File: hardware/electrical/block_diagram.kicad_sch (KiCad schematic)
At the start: 0 parts

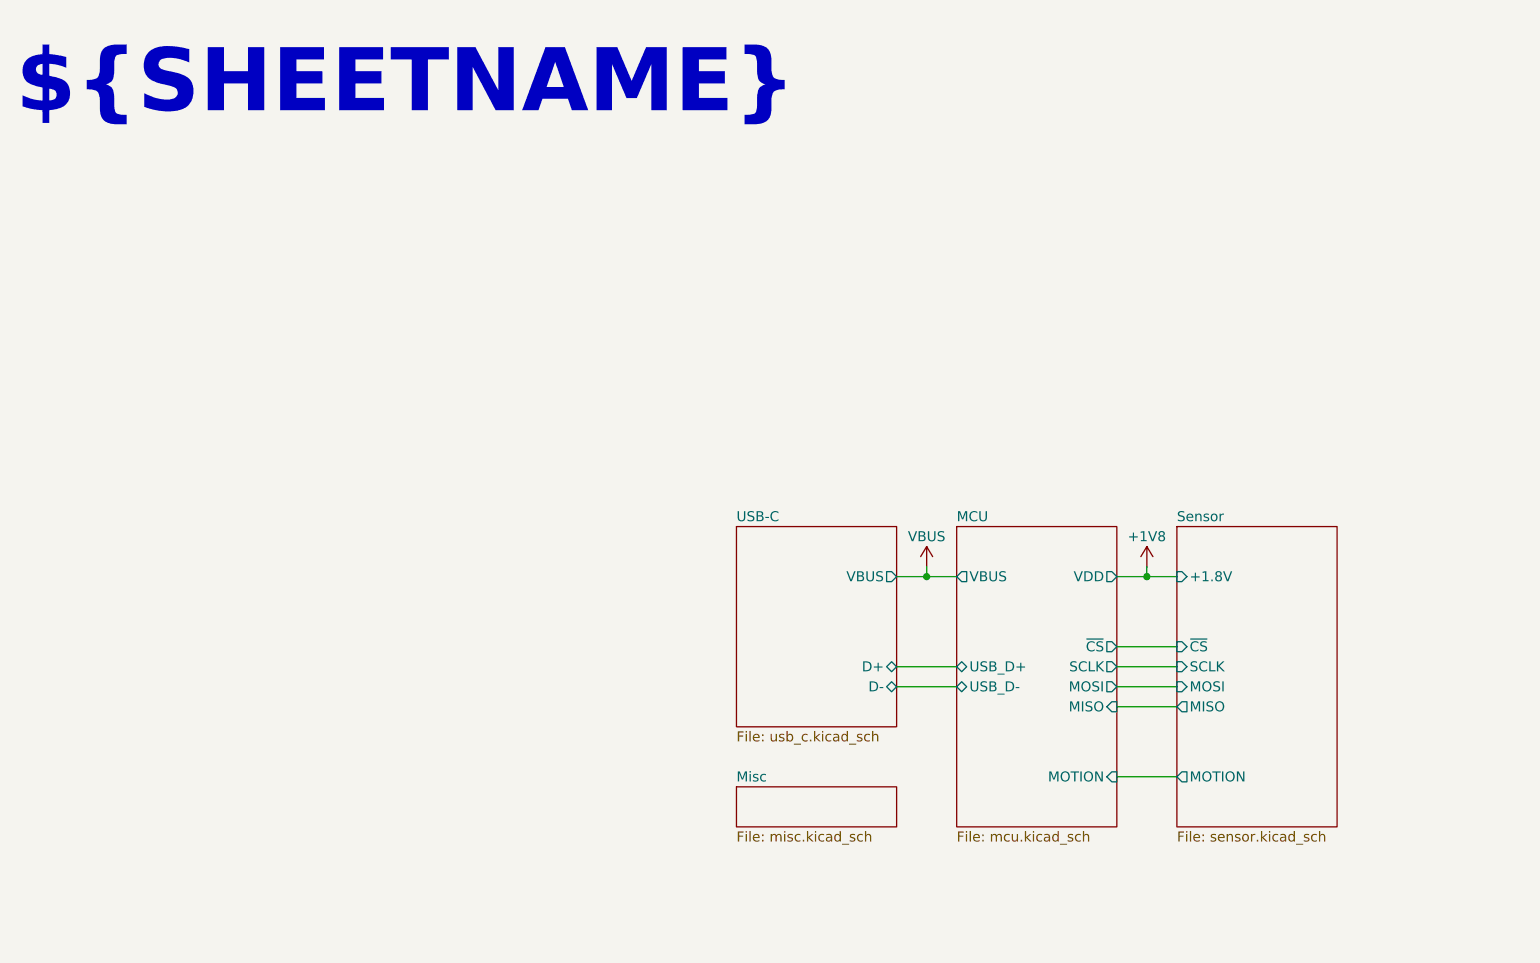
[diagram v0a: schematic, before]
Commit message: Update schematic to include regulators and switches, update render
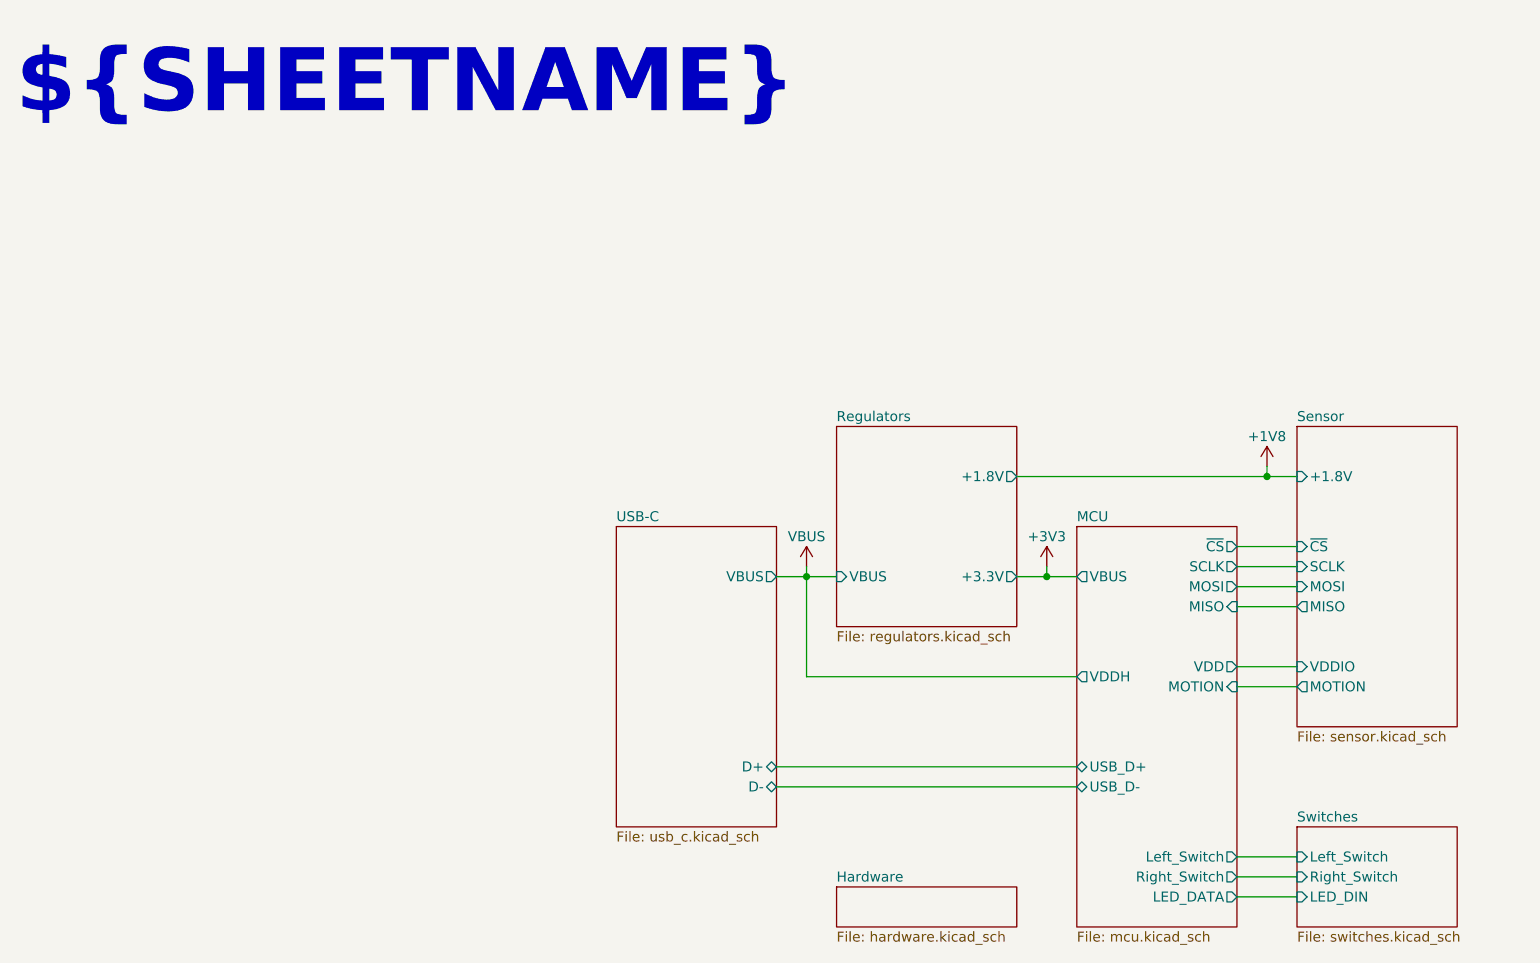
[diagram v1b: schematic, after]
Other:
- sheet Misc renamed Hardware
- added sheet Regulators (regulators.kicad_sch)
- added sheet Switches (switches.kicad_sch)
- sheet Hardware: file misc.kicad_sch -> hardware.kicad_sch
- sheet MCU ports: added LED_DATA, Left_Switch, Right_Switch, VDDH; removed none
- sheet Sensor ports: added VDDIO; removed none
